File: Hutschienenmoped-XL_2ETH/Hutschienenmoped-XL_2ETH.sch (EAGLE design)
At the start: 129 parts, among them J1 638207222005, J13 638207222005, J15 638207222008, J2 645004114822, J4 61300421121, J7 638207222005, J8 638207222007, U4 TLE9250VSJ

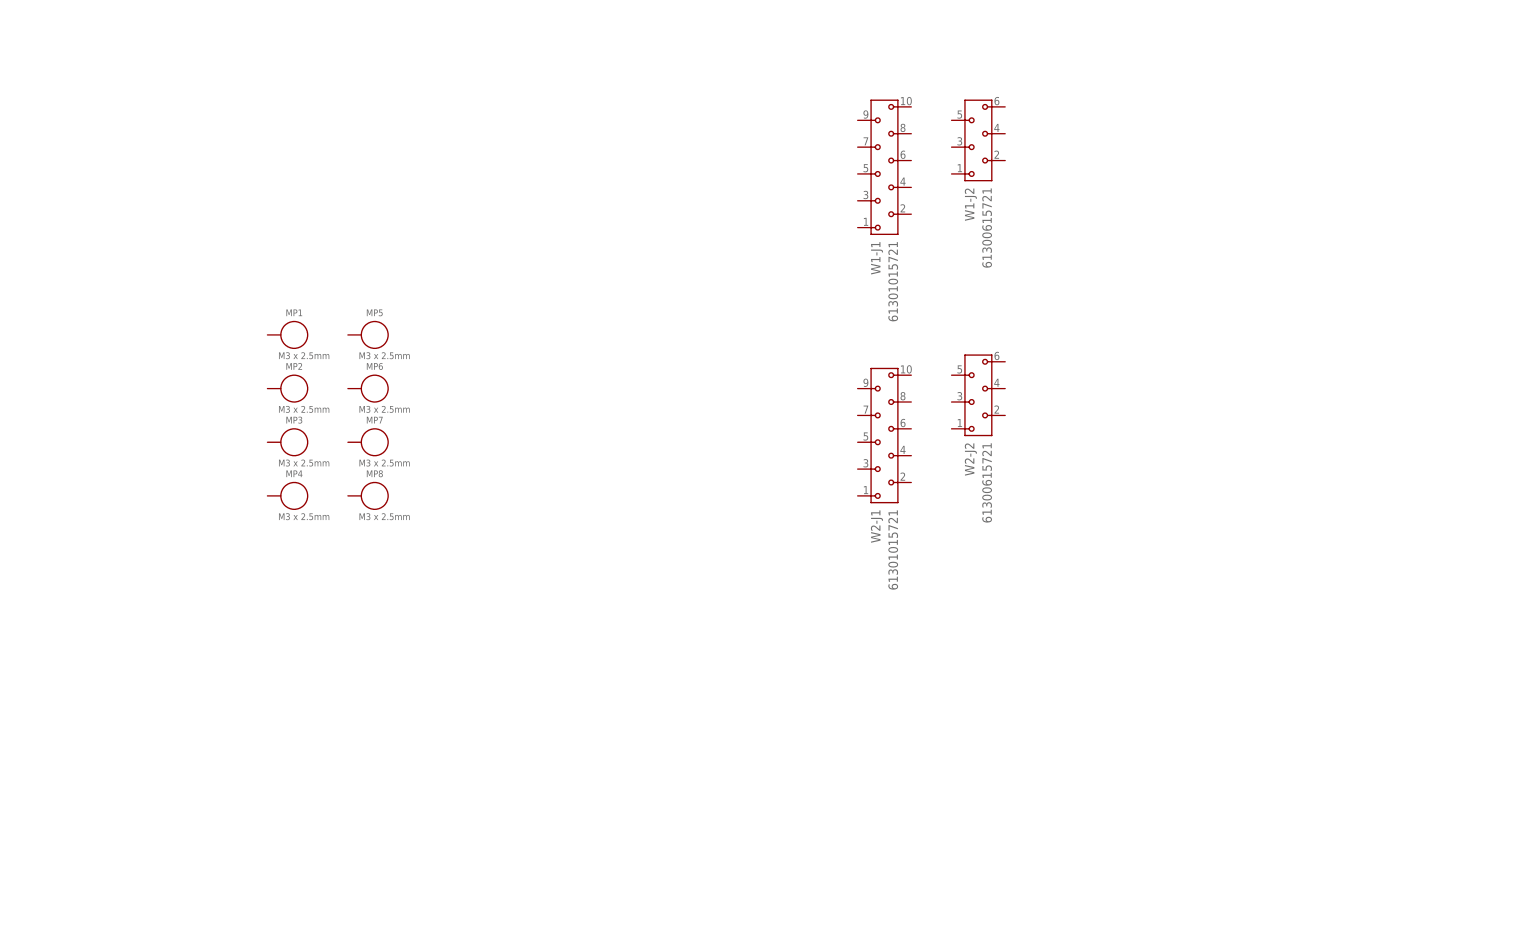
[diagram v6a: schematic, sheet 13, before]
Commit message: Update package description and pad positions, adjust hole sizes, and modify parameters for better PCB design. Add new contact references, wires, and signals for improved connectivity.
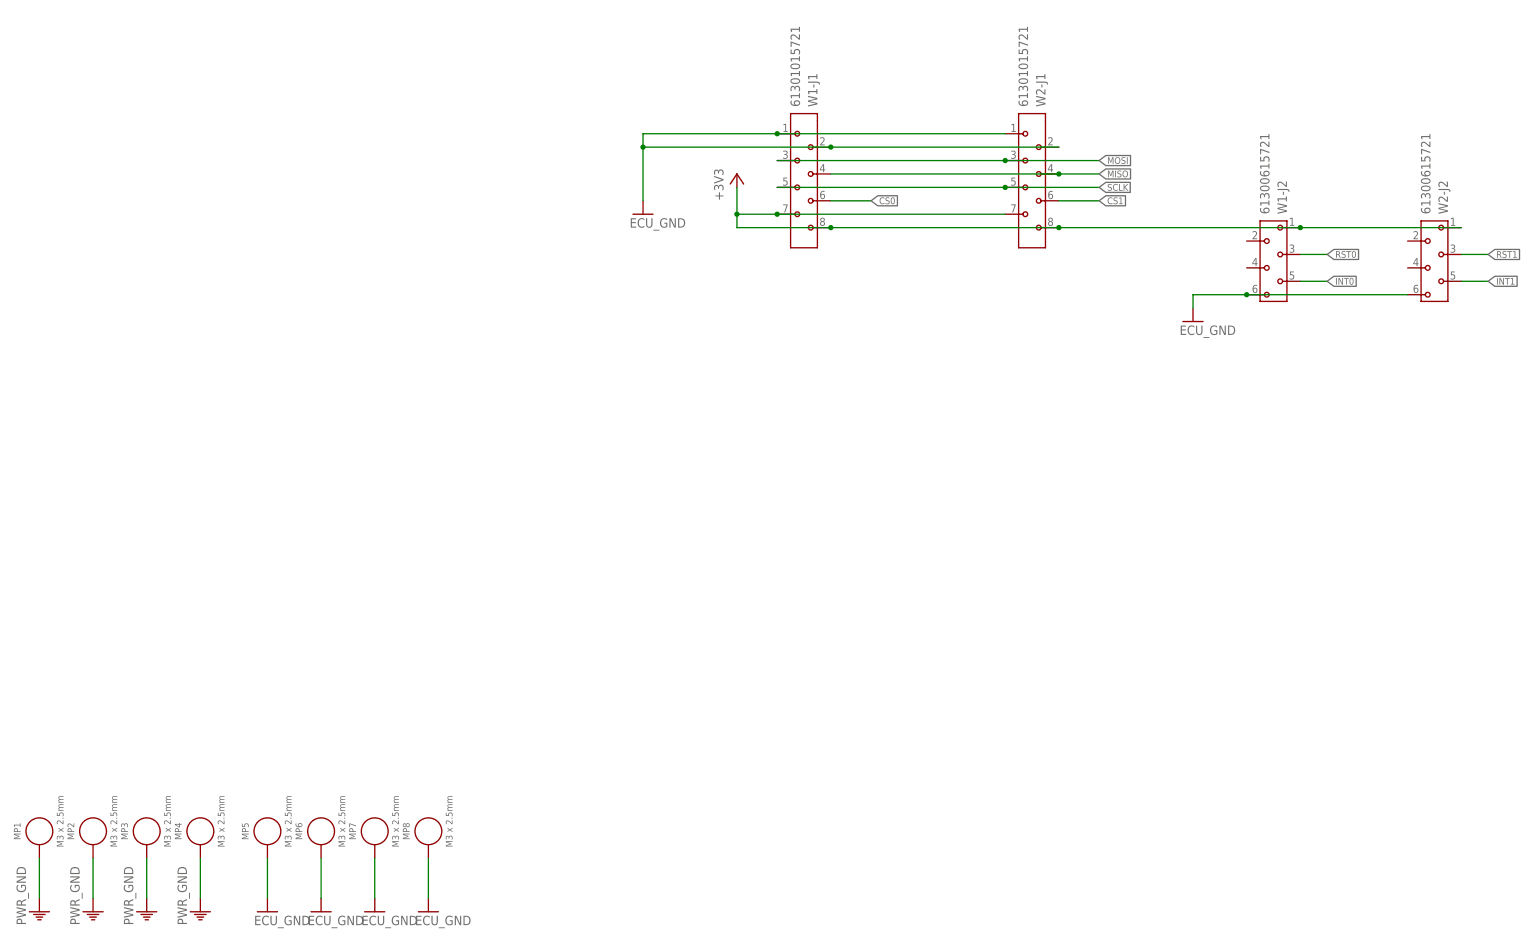
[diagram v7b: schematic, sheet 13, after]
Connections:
- new net CS0: W1-J1.6
- new net CS1: W2-J1.6
- new net INT0: W1-J2.5
- new net INT1: W2-J2.5
- new net MISO: W1-J1.4, W2-J1.4
- new net MOSI: W1-J1.3, W2-J1.3
- new net RST0: W1-J2.3
- new net RST1: W2-J2.3
- new net SCLK: W1-J1.5, W2-J1.5
- net +3V3: now also W1-J1.7, W1-J1.8, W1-J2.1, W2-J1.7, W2-J1.8, W2-J2.1
- net ECU_GND: now also MP5.1, MP6.1, MP7.1, MP8.1, W1-J1.1, W1-J1.2, W1-J2.6, W2-J1.1, W2-J1.2, W2-J2.6
- net PWR_GND: now also MP1.1, MP2.1, MP3.1, MP4.1
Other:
- moved on the sheet: MP1, MP2, MP3, MP4, MP5, MP6, MP7, MP8, W1-J2, W2-J2

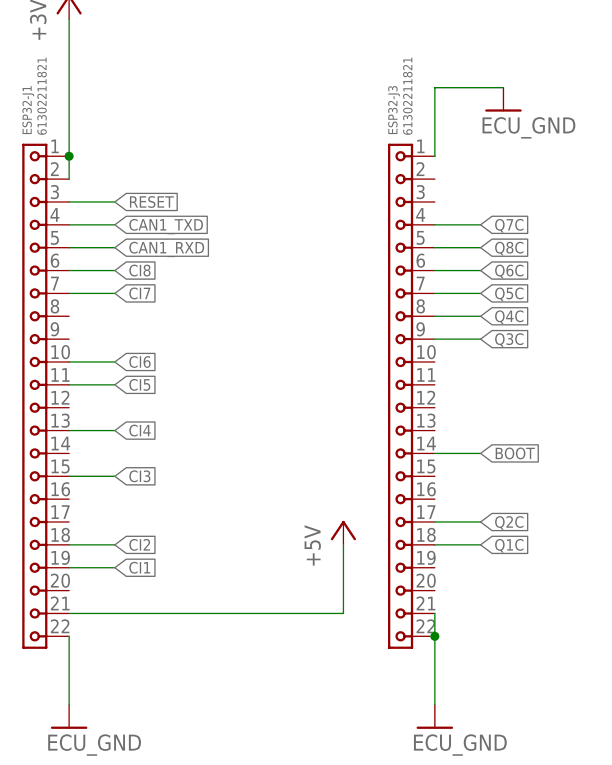
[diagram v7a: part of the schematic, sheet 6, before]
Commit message: Update Fusion 360 sync details and add new signal connections. Add text labels for USB, PRG, and PSRAM on the schematic sheet.
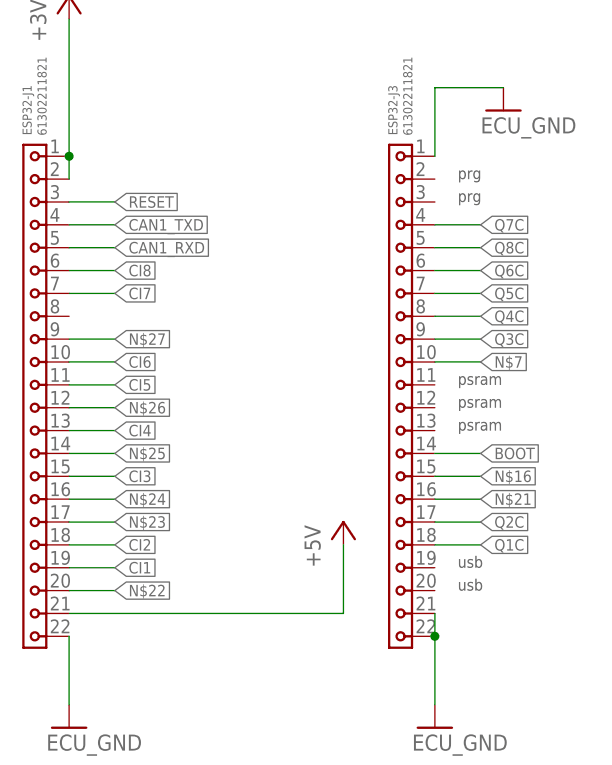
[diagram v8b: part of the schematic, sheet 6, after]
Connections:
- new net N$16: ESP32-J3.15
- new net N$21: ESP32-J3.16
- new net N$22: ESP32-J1.20
- new net N$23: ESP32-J1.17
- new net N$24: ESP32-J1.16
- new net N$25: ESP32-J1.14
- new net N$26: ESP32-J1.12
- new net N$27: ESP32-J1.9
- new net N$7: ESP32-J3.10
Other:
- note added: "prg"
- note added: "psram"
- note added: "usb"
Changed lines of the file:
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@@
 <sheet>
 <plain>
+<text x="147.32" y="83.82" size="1.27" layer="97">usb</text>
+<text x="147.32" y="81.28" size="1.27" layer="97">usb</text>
+<text x="147.32" y="127" size="1.27" layer="97">prg</text>
+<text x="147.32" y="124.46" size="1.27" layer="97">prg</text>
+<text x="147.32" y="104.14" size="1.27" layer="97">psram</text>
+<text x="147.32" y="101.6" size="1.27" layer="97">psram</text>
+<text x="147.32" y="99.06" size="1.27" layer="97">psram</text>
 </plain>
 <instances>
@@
 </segment>
 </net>
+<net name="N$7" class="0">
+<segment>
+<pinref part="ESP32-J3" gate="G$1" pin="10"/>
+<wire x1="144.78" y1="106.68" x2="149.86" y2="106.68" width="0.1524" layer="91"/>
+<label x="149.86" y="106.68" size="1.27" layer="95" xref="yes"/>
+</segment>
+</net>
+<net name="N$16" class="0">
+<segment>
+<pinref part="ESP32-J3" gate="G$1" pin="15"/>
+<wire x1="144.78" y1="93.98" x2="149.86" y2="93.98" width="0.1524" layer="91"/>
+<label x="149.86" y="93.98" size="1.27" layer="95" xref="yes"/>
+</segment>
+</net>
+<net name="N$21" class="0">
+<segment>
+<pinref part="ESP32-J3" gate="G$1" pin="16"/>
+<wire x1="144.78" y1="91.44" x2="149.86" y2="91.44" width="0.1524" layer="91"/>
+<label x="149.86" y="91.44" size="1.27" layer="95" xref="yes"/>
+</segment>
+</net>
+<net name="N$22" class="0">
+<segment>
+<pinref part="ESP32-J1" gate="G$1" pin="20"/>
+<wire x1="104.14" y1="81.28" x2="109.22" y2="81.28" width="0.1524" layer="91"/>
+<label x="109.22" y="81.28" size="1.27" layer="95" xref="yes"/>
+</segment>
+</net>
+<net name="N$23" class="0">
+<segment>
+<pinref part="ESP32-J1" gate="G$1" pin="17"/>
+<wire x1="104.14" y1="88.9" x2="109.22" y2="88.9" width="0.1524" layer="91"/>
+<label x="109.22" y="88.9" size="1.27" layer="95" xref="yes"/>
+</segment>
+</net>
+<net name="N$24" class="0">
+<segment>
+<pinref part="ESP32-J1" gate="G$1" pin="16"/>
+<wire x1="104.14" y1="91.44" x2="109.22" y2="91.44" width="0.1524" layer="91"/>
+<label x="109.22" y="91.44" size="1.27" layer="95" xref="yes"/>
+</segment>
+</net>
+<net name="N$25" class="0">
+<segment>
+<pinref part="ESP32-J1" gate="G$1" pin="14"/>
+<wire x1="104.14" y1="96.52" x2="109.22" y2="96.52" width="0.1524" layer="91"/>
+<label x="109.22" y="96.52" size="1.27" layer="95" xref="yes"/>
+</segment>
+</net>
+<net name="N$26" class="0">
+<segment>
+<pinref part="ESP32-J1" gate="G$1" pin="12"/>
+<wire x1="104.14" y1="101.6" x2="109.22" y2="101.6" width="0.1524" layer="91"/>
+<label x="109.22" y="101.6" size="1.27" layer="95" xref="yes"/>
+</segment>
+</net>
+<net name="N$27" class="0">
+<segment>
+<pinref part="ESP32-J1" gate="G$1" pin="9"/>
+<wire x1="104.14" y1="109.22" x2="109.22" y2="109.22" width="0.1524" layer="91"/>
+<label x="109.22" y="109.22" size="1.27" layer="95" xref="yes"/>
+</segment>
+</net>
